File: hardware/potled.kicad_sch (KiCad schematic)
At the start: 29 parts, among them U1 TL072, U2 TL072

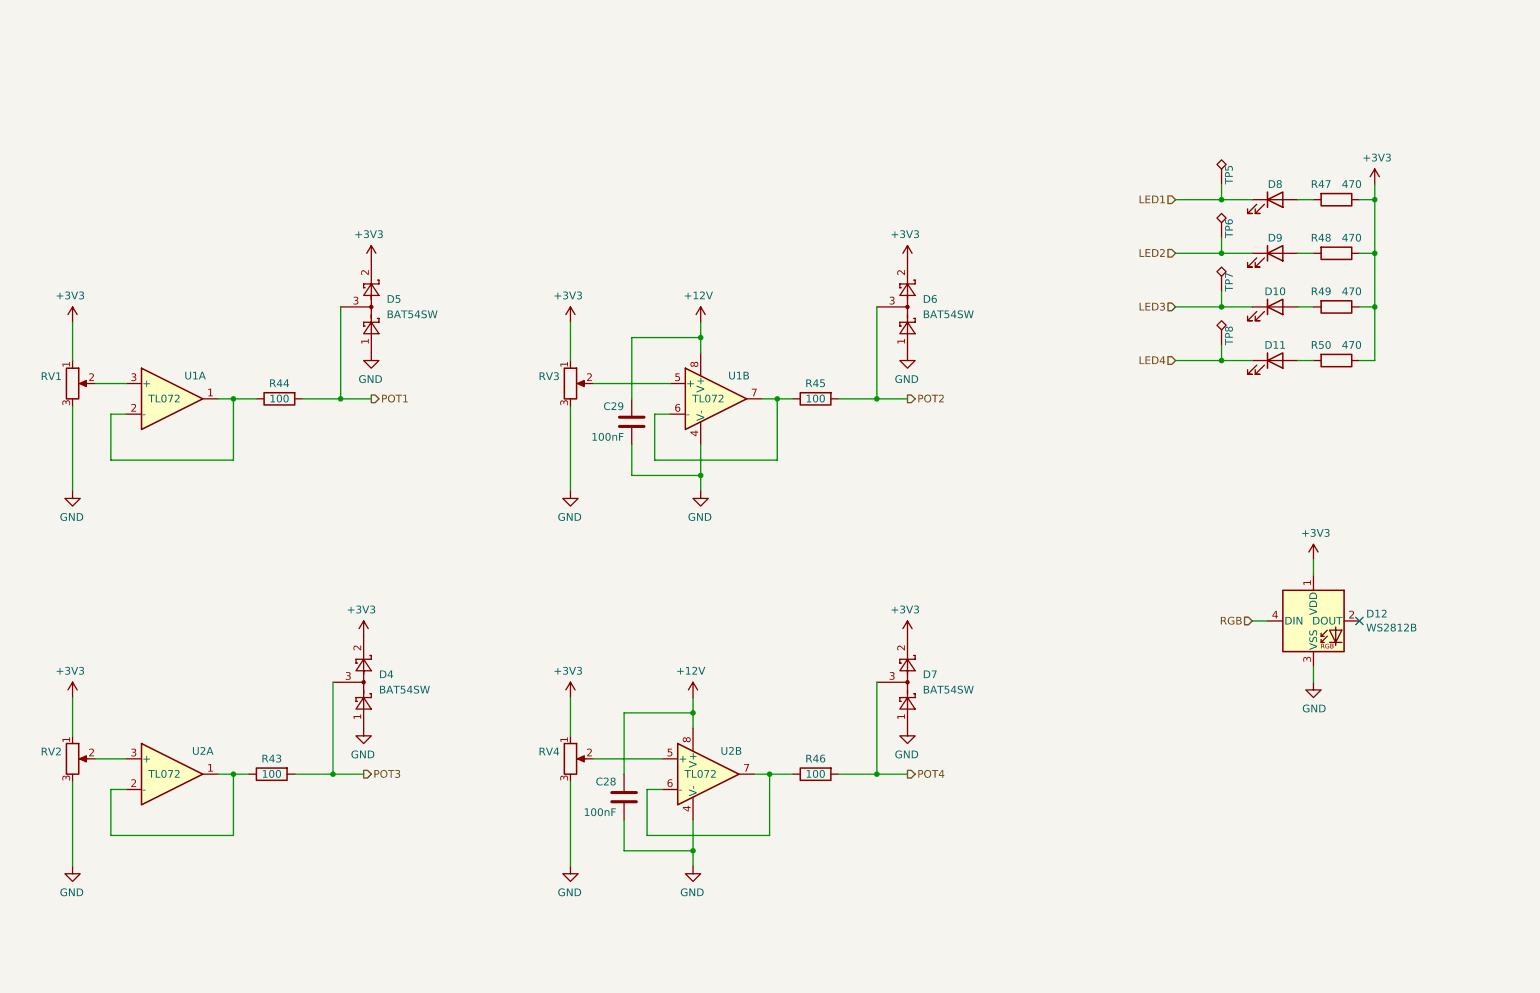
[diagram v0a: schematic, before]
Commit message: First cut of the software. Not changed to RISC-V yet.
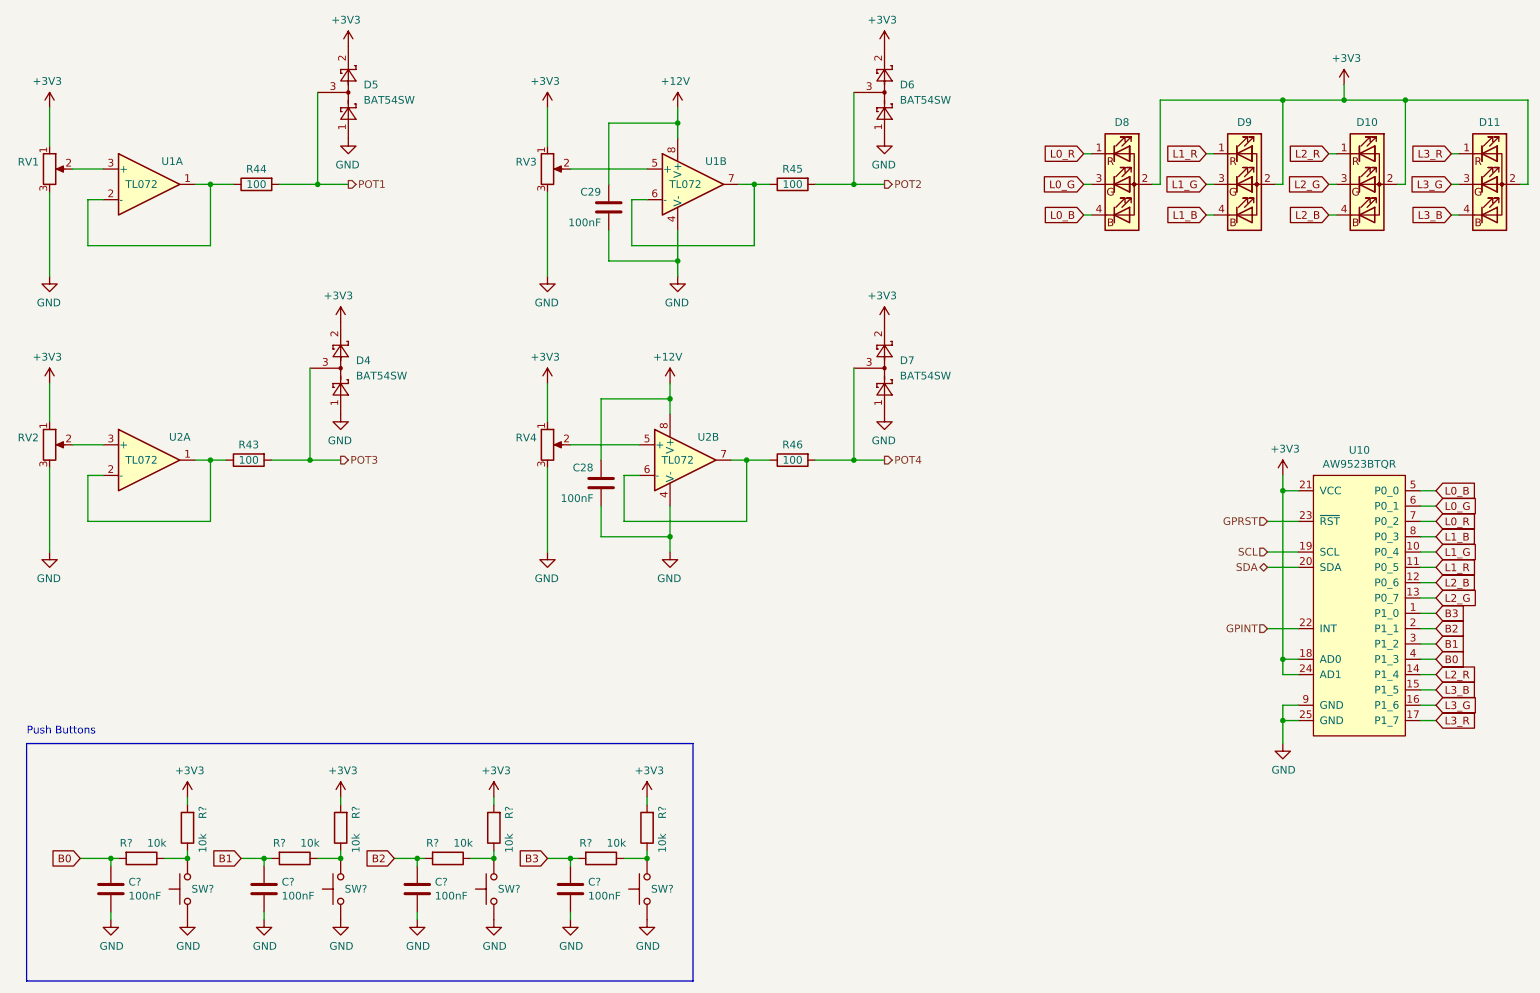
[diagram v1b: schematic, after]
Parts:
- removed D10, D11, D8, D9: ~, LED_THT:LED_D3.0mm, symbol Device:LED
- removed D12: WS2812B, LED_SMD:LED_WS2812B_PLCC4_5.0x5.0mm_P3.2mm, symbol LED:WS2812B
- removed R47, R48, R49, R50: 470, Resistor_SMD:R_0603_1608Metric, symbol Device:R
- removed TP5, TP6, TP7, TP8: ~, aaa:TestPoint_THTPad_1.0x1.0mm_Drill0.6mm, symbol Connector:TestPoint_Alt
- added C? (x4): 100nF, Capacitor_SMD:C_0603_1608Metric, symbol Device:C
- added D10, D11, D8, D9: ~, LED_THT:LED_D5.0mm-4_RGB, symbol Device:LED_RAGB
- added R? (x8): 10k, Resistor_SMD:R_0603_1608Metric, symbol Device:R
- added SW? (x4): ~, Button_Switch_THT:SW_PUSH_6mm_H8mm, symbol Switch:SW_Push
- added U10: AW9523BTQR, Package_DFN_QFN:VQFN-24-1EP_4x4mm_P0.5mm_EP2.45x2.45mm, symbol aaa:AW9523BTQR
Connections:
- net +3V3: now also D10.2 (A), D11.2 (A), D8.2 (A), D9.2 (A), R?.2, R?.2, R?.2, R?.2, U10.18 (AD0), U10.21 (VCC), U10.24 (AD1)
- net GND: now also C?.2, C?.2, C?.2, C?.2, SW?.1, SW?.1, SW?.1, SW?.1, U10.25 (GND), U10.9 (GND)
- new net: R?.1, R?.1, SW?.2 (x4)
- new net B0: C?.1, R?.2, U10.4 (P1_3)
- new net B1: C?.1, R?.2, U10.3 (P1_2)
- new net B2: C?.1, R?.2, U10.2 (P1_1)
- new net B3: C?.1, R?.2, U10.1 (P1_0)
- new net GPINT: U10.22 (INT)
- new net GPRST: U10.23 (~{RST})
- new net L0_B: D8.4 (BK), U10.5 (P0_0)
- new net L0_G: D8.3 (GK), U10.6 (P0_1)
- new net L0_R: D8.1 (RK), U10.7 (P0_2)
- new net L1_B: D9.4 (BK), U10.8 (P0_3)
- new net L1_G: D9.3 (GK), U10.10 (P0_4)
- new net L1_R: D9.1 (RK), U10.11 (P0_5)
- new net L2_B: D10.4 (BK), U10.12 (P0_6)
- new net L2_G: D10.3 (GK), U10.13 (P0_7)
- new net L2_R: D10.1 (RK), U10.14 (P1_4)
- new net L3_B: D11.4 (BK), U10.15 (P1_5)
- new net L3_G: D11.3 (GK), U10.16 (P1_6)
- new net L3_R: D11.1 (RK), U10.17 (P1_7)
- new net SCL: U10.19 (SCL)
- new net SDA: U10.20 (SDA)
- no-connect marks 1 -> 0
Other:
- note added: "Push Buttons"
- moved on the sheet: C28, C29, D4, D5, D6, D7, R43, R44, R45, R46, RV1, RV2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
